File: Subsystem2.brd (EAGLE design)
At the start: 100 x 80 mm, 22 parts

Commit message: add 3232 external caps
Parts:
- added C2, C3, C4, C5, C6: 0.1uF, Brendan:0805
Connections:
- new net M32_C1+: C2.1, U$2.1
- new net M32_C1-: C2.2, U$2.3
- new net M32_C2+: C3.1, U$2.4
- new net M32_C2-: C3.2, U$2.5
- new net M32_V+: C5.1, U$2.2
- new net M32_V-: C4.1, U$2.6
- net 3.3V: now also C6.1, U$2.16
- net GND: now also C4.2, C5.2, C6.2
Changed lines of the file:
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@@
 <attribute name="OC_FARNELL" value="unknown" x="-6.35" y="-11.43" size="1.778" layer="27" display="off"/>
 </element>
+<element name="C2" library="Brendan" package="0805" value="0.1uF" x="-13.97" y="-11.43"/>
+<element name="C3" library="Brendan" package="0805" value="0.1uF" x="-17.78" y="-11.43"/>
+<element name="C4" library="Brendan" package="0805" value="0.1uF" x="-21.59" y="-11.43"/>
+<element name="C5" library="Brendan" package="0805" value="0.1uF" x="-25.4" y="-11.43"/>
+<element name="C6" library="Brendan" package="0805" value="0.1uF" x="-29.21" y="-11.43"/>
 </elements>
 <signals>
@@
 <wire x1="93.98" y1="23.495" x2="92.01" y2="23.495" width="0.4064" layer="1"/>
 <wire x1="92.01" y1="23.495" x2="92" y2="23.485" width="0.4064" layer="1"/>
+<contactref element="C5" pad="2"/>
+<contactref element="C4" pad="2"/>
+<contactref element="C6" pad="2"/>
+<wire x1="-24.5" y1="-11.43" x2="-28.31" y2="-11.43" width="0" layer="19" extent="1-1"/>
+<wire x1="-20.69" y1="-11.43" x2="-24.5" y2="-11.43" width="0" layer="19" extent="1-1"/>
+<wire x1="12.7" y1="24.615" x2="-20.69" y2="-11.43" width="0" layer="19" extent="1-1"/>
 </signal>
 <signal name="N$4">
@@
 <wire x1="75.565" y1="54.2925" x2="77.47" y2="54.2925" width="0.4064" layer="1"/>
 <wire x1="77.47" y1="54.2925" x2="77.47" y2="54.61" width="0.4064" layer="1"/>
+<contactref element="U$2" pad="16"/>
+<contactref element="C6" pad="1"/>
+<wire x1="-10.795" y1="11.7475" x2="-30.11" y2="-11.43" width="0" layer="19" extent="1-1"/>
+<wire x1="9.8425" y1="23.1775" x2="-10.795" y2="11.7475" width="0" layer="19" extent="1-1"/>
 </signal>
 <signal name="PWM1">
@@
 <wire x1="-6.985" y1="11.7475" x2="-8.89" y2="-5.08" width="0" layer="19" extent="1-1"/>
 </signal>
+<signal name="M32_C1+">
+<contactref element="U$2" pad="1"/>
+<contactref element="C2" pad="1"/>
+<wire x1="-10.795" y1="3.4925" x2="-14.87" y2="-11.43" width="0" layer="19" extent="1-1"/>
+</signal>
+<signal name="M32_C1-">
+<contactref element="C2" pad="2"/>
+<contactref element="U$2" pad="3"/>
+<wire x1="-8.255" y1="3.4925" x2="-13.07" y2="-11.43" width="0" layer="19" extent="1-1"/>
+</signal>
+<signal name="M32_C2+">
+<contactref element="U$2" pad="4"/>
+<contactref element="C3" pad="1"/>
+<wire x1="-6.985" y1="3.4925" x2="-18.68" y2="-11.43" width="0" layer="19" extent="1-1"/>
+</signal>
+<signal name="M32_C2-">
+<contactref element="C3" pad="2"/>
+<contactref element="U$2" pad="5"/>
+<wire x1="-5.715" y1="3.4925" x2="-16.88" y2="-11.43" width="0" layer="19" extent="1-1"/>
+</signal>
+<signal name="M32_V-">
+<contactref element="U$2" pad="6"/>
+<contactref element="C4" pad="1"/>
+<wire x1="-4.445" y1="3.4925" x2="-22.49" y2="-11.43" width="0" layer="19" extent="1-1"/>
+</signal>
+<signal name="M32_V+">
+<contactref element="U$2" pad="2"/>
+<contactref element="C5" pad="1"/>
+<wire x1="-9.525" y1="3.4925" x2="-26.3" y2="-11.43" width="0" layer="19" extent="1-1"/>
+</signal>
 </signals>

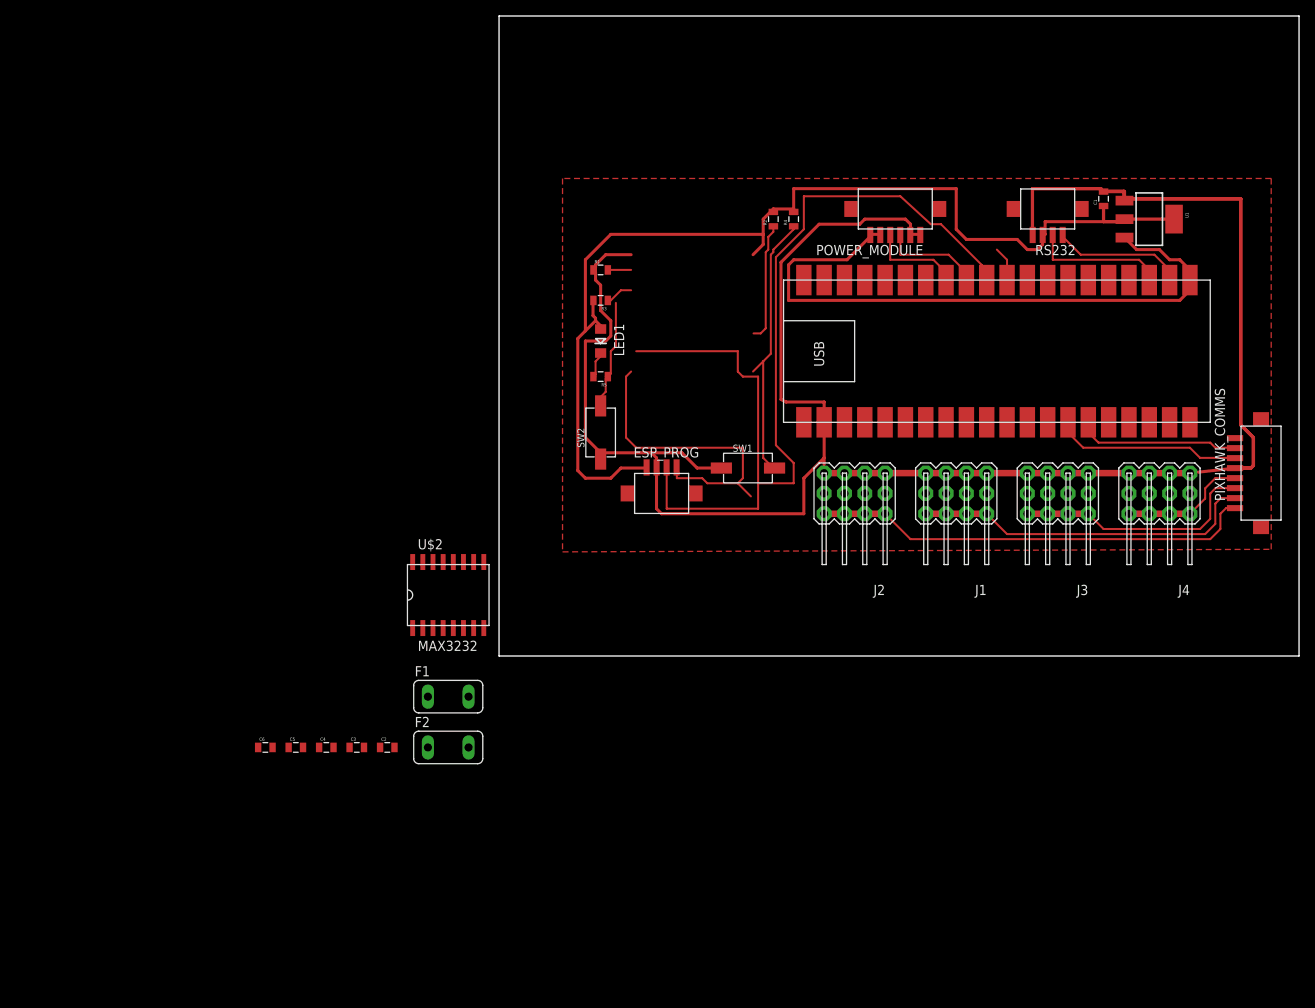
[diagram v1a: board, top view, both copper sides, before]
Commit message: finish first-draft schematic of v2 board
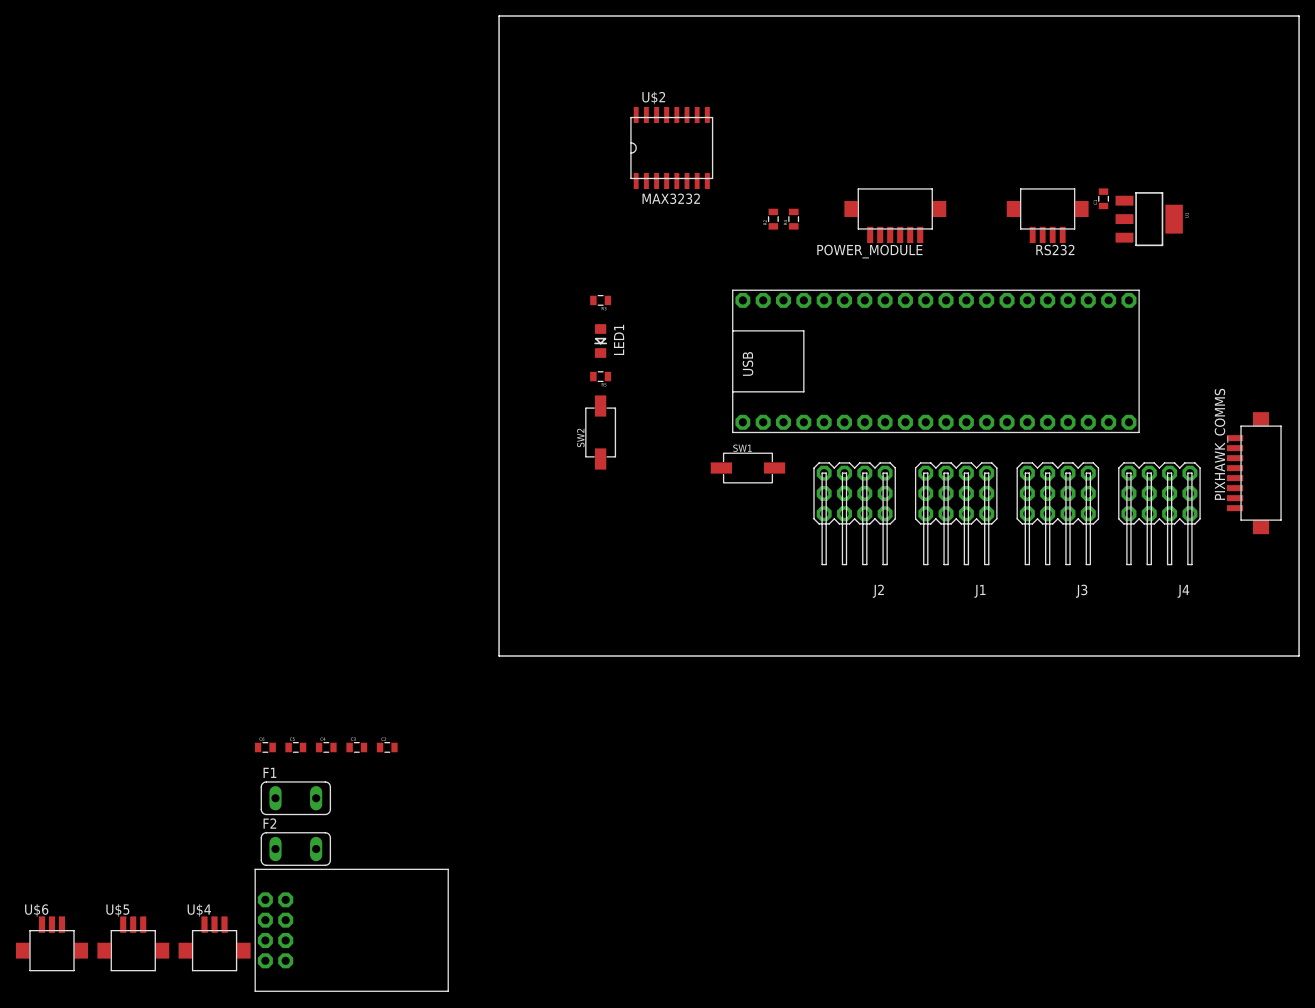
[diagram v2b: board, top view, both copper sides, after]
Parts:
- removed ESP_PROG: 4PIN-PLUG, Brendan:4PIN-PLUG
- removed R1: 10k, Brendan:0805
- added U$3: ESP-01, Brendan:ESP-01
- added U$4, U$5, U$6: 3PIN-PLUG, Brendan:3PIN-PLUG
- U$1: value MAPLE-MINI -> MAPLE-MINI-SOCKET; device Brendan:MAPLE-MINI -> Brendan:MAPLE-MINI-SOCKET
- moved U$2 62.5 mm to (21.6, 63.5)
- moved F1 22.9 mm to (-25.4, -17.8)
- moved F2 22.9 mm to (-25.4, -24.1)
- moved U$1 7.73 mm to (54.6, 36.8)
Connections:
- removed net GPIO15: R1.2
- new net N$5: U$1.P$4
- new net SENSE1: U$1.P$5, U$4.P$2
- new net SENSE2: U$1.P$6, U$5.P$2
- new net SENSE3: U$1.P$7, U$6.P$2
- net 3.3V: now also U$3.4, U$4.P$1, U$5.P$1, U$6.P$1; no longer ESP_PROG.P$1
- net CH_PD: now also U$3.2
- net GND: now also U$3.8, U$4.P$3, U$5.P$3, U$6.P$3; no longer ESP_PROG.P$2, R1.1
- net GPIO0: now also U$3.6
- net GPIO2: now also U$3.7
- net RESET: now also U$3.3
- net RX2: now also U$3.1; no longer ESP_PROG.P$4
- net TX2: now also U$3.5; no longer ESP_PROG.P$3
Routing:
- net GND: track 270.8 -> 0.00 mm
- net 3.3V: track 139.6 -> 0.00 mm
- net TX2: track 121.7 -> 0.00 mm
- net 5V: track 80.8 -> 0.00 mm
- net PWM3: track 55.4 -> 0.00 mm
- net N$1: track 50.3 -> 0.00 mm
- net RX2: track 44.2 -> 0.00 mm
- net PWM4: track 43.1 -> 0.00 mm
- net RESET: track 34.3 -> 0.00 mm
- net PWM2: track 30.7 -> 0.00 mm
- net RX1: track 23.5 -> 0.00 mm
- net TX1: track 20.4 -> 0.00 mm
- net TX3: track 16.7 -> 0.00 mm
- net RX3: track 16.3 -> 0.00 mm
- net PWM1: track 15.8 -> 0.00 mm
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- removed copper zone on layer 1, net GND
